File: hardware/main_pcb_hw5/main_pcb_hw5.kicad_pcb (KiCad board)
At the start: 2 copper layers, 100 x 100 mm, 31 parts, among them J1 MEGA BOTTOM, J10 GBA_Slot, J3 CART SLOT TOP ROW, J4 CART SLOT FRONT ROW, J6 5V USB, J7 Conn_01x07, J8 EXP2, J9 EXP1, M2_1 Screw_Terminal_01x01, M2_2 Screw_Terminal_01x01, M2_3 Screw_Terminal_01x01, M2_4 Screw_Terminal_01x01, M2_5 Screw_Terminal_01x01, M2_6 Screw_Terminal_01x01, M2_7 Screw_Terminal_01x01, M2_8 Screw_Terminal_01x01, M2_9 Screw_Terminal_01x01, SW1 VOLTAGE, SW2 POWER, U1 TPS2113PW, U2 DS3231MZ

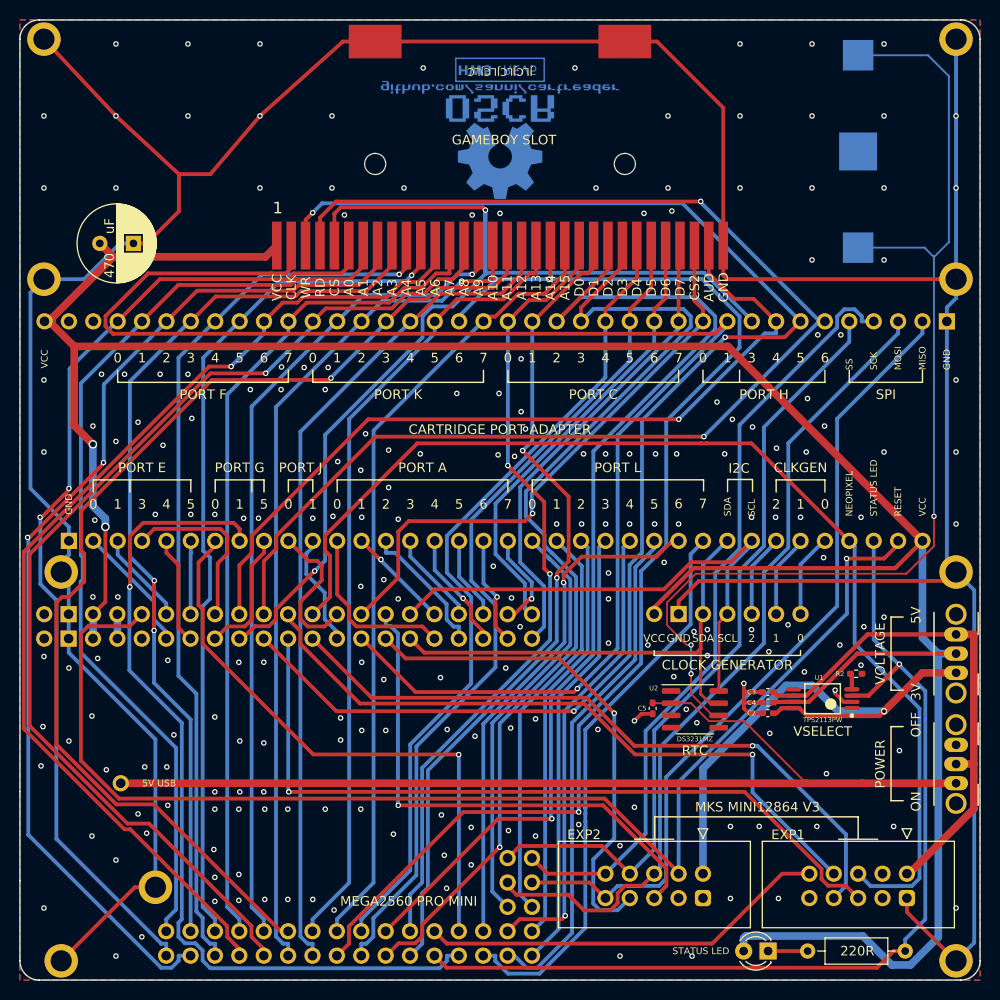
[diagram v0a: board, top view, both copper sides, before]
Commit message: Changed 0402 components to 0603
 - Also tweaked name in board graphics to make it clear this isn't a
   vanilla board.
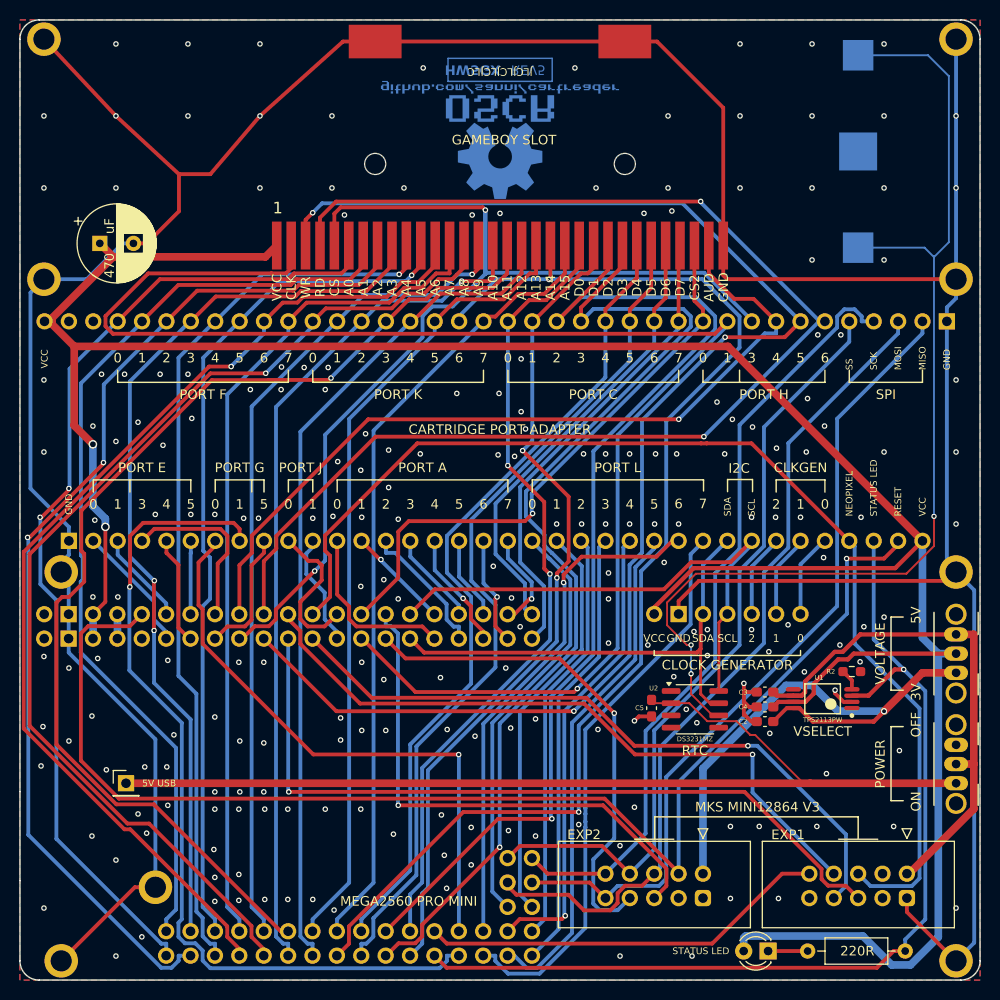
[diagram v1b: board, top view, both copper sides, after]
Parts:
- C2, C3, C4, C5: footprint Capacitor_SMD:C_0402_1005Metric_Pad0.74x0.62mm_HandSolder -> Capacitor_SMD:C_0603_1608Metric_Pad1.08x0.95mm_HandSolder
- R2: footprint Resistor_SMD:R_0402_1005Metric_Pad0.72x0.64mm_HandSolder -> Resistor_SMD:R_0603_1608Metric_Pad0.98x0.95mm_HandSolder
- moved C2 0.93 mm to (177.6, 123.1)
- moved J6 0.55 mm to (111.0, 129.5)
- moved C4 0.54 mm to (177.6, 121.6)
- moved R2 0.52 mm to (186.6, 117.9)
- moved C3 0.30 mm to (177.6, 120.0)
- moved C5 0.12 mm to (165.8, 121.7)
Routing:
- net GND: track 382.8 -> 377.1 mm
- net A8: track 113.4 -> 110.6 mm
- net A4: track 94.1 -> 91.7 mm
- net D36: track 86.3 -> 84.0 mm
- net A1: track 98.4 -> 96.2 mm
- net D37: track 83.4 -> 81.2 mm
- net A0: track 103.9 -> 101.7 mm
- net A2: track 109.6 -> 107.4 mm
- net D34: track 107.1 -> 104.9 mm
- net A3: track 94.3 -> 92.2 mm
- net A5: track 89.6 -> 87.5 mm
- net A6: track 109.7 -> 107.7 mm
- net +3V3: track 56.0 -> 56.8 mm
- net VCC: track 282.8 -> 283.6 mm
- net D9: track 136.0 -> 135.3 mm
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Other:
- board text added: "HW5GX"
- board text removed: "HW5"

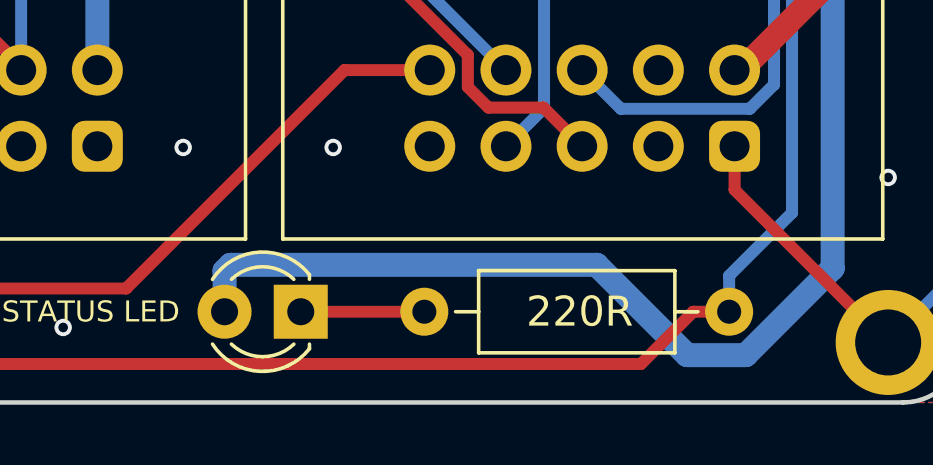
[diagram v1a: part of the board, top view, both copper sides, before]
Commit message: Made LED and its resistor SMD, added teardrops
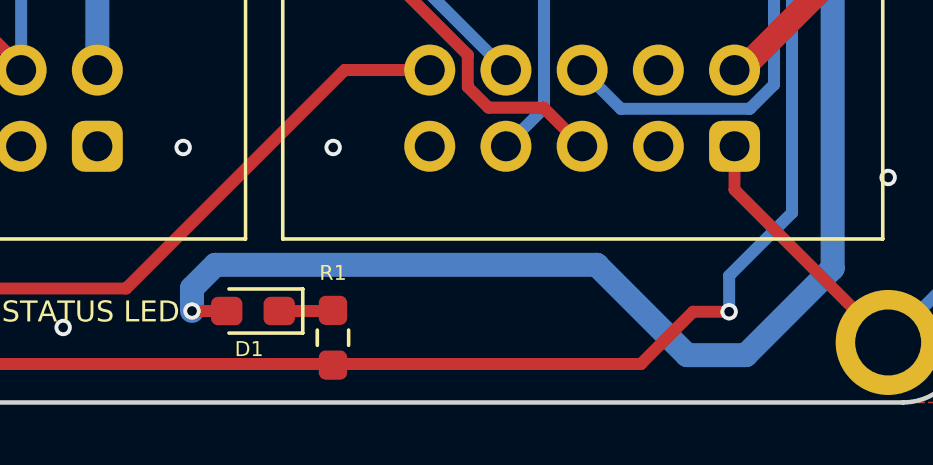
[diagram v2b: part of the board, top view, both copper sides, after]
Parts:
- D1: footprint LED_THT:LED_D3.0mm -> LED_SMD:LED_0603_1608Metric_Pad1.05x0.95mm_HandSolder
- R1: value 220R -> 1k; footprint Resistor_THT:R_Axial_DIN0207_L6.3mm_D2.5mm_P10.16mm_Horizontal -> Resistor_SMD:R_0603_1608Metric_Pad0.98x0.95mm_HandSolder
- moved R1 3.17 mm to (179.0, 147.8), turned to -90 degrees
- moved D1 1.59 mm to (176.3, 147.0)
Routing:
- net Net-(D1-K): track 4.12 -> 1.80 mm
- net VCC: track 283.6 -> 285.6 mm, vias 2 -> 3
- net D38: vias 1 -> 2
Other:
- board text removed: "220R"
